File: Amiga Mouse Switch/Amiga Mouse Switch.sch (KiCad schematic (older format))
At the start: 23 parts, among them J1 JOYSTICK, J2 Mouse, J3 Amiga IDC, M1 Mounting, M2 Mounting, M3 Mounting, M4 Mounting, SW1 JOY_SEL, SW2 MOUSE_SEL, U1 74HCT4053, U2 74HCT4053, U3 NE555

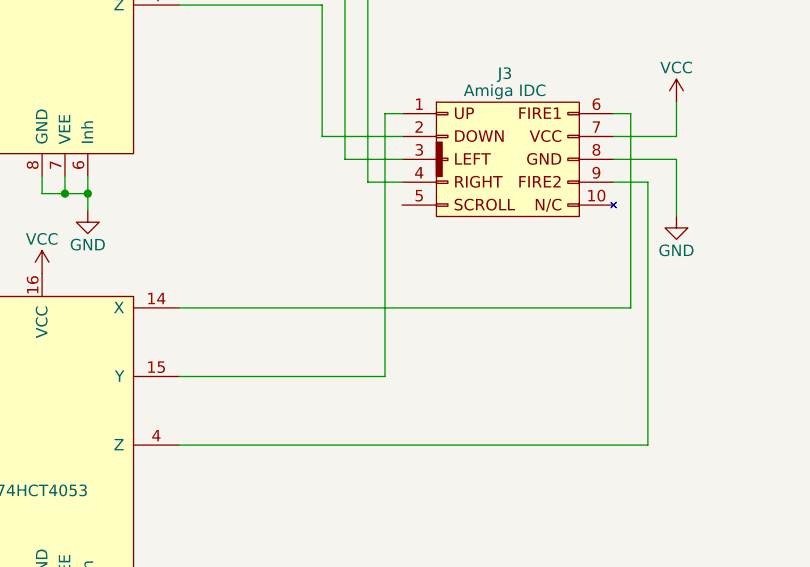
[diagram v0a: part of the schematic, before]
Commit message: Added diode for lines that have pull-ups onboard
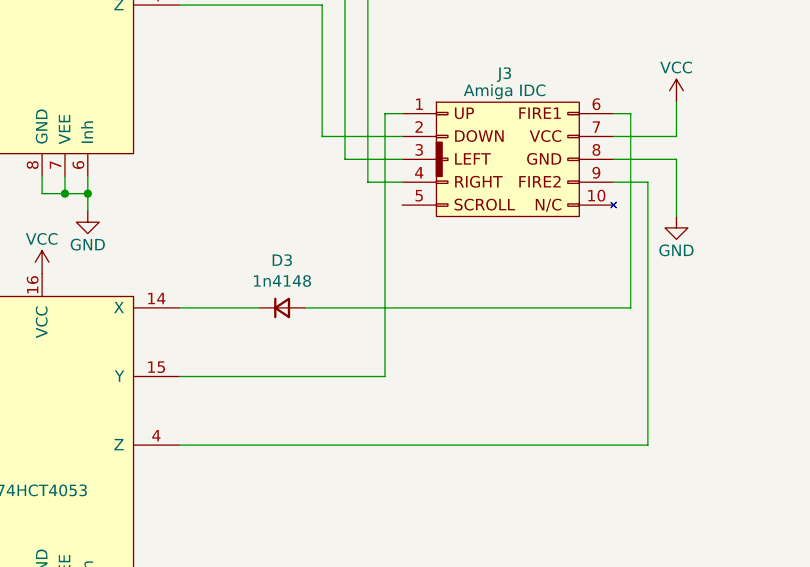
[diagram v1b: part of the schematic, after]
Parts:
- added D3: 1n4148, Diode_THT:D_DO-35_SOD27_P7.62mm_Horizontal, symbol Device:D_Small
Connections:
- net at U2.14 (X): now also D3.1 (K); no longer J3.6 (Pin_6)
- new net: D3.2 (A), J3.6 (Pin_6)
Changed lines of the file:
@@
 	6550 2475 6475 2475
 Wire Wire Line
-	4575 3325 6550 3325
+	4575 3325 4925 3325
 Wire Wire Line
 	6475 2775 6625 2775
@@
 Wire Wire Line
 	3525 6325 2600 6325
+$Comp
+L Device:D_Small D3
+U 1 1 604A3E07
+P 5025 3325
+F 0 "D3" H 5025 3532 50  0000 C CNN
+F 1 "1n4148" H 5025 3441 50  0000 C CNN
+F 2 "Diode_THT:D_DO-35_SOD27_P7.62mm_Horizontal" V 5025 3325 50  0001 C CNN
+F 3 "~" V 5025 3325 50  0001 C CNN
+	1    5025 3325
+	1    0    0    -1
+$EndComp
+Wire Wire Line
+	5125 3325 6550 3325
 $EndSCHEMATC

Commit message: Fixed RMB
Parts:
- added D4: 1n4148, Diode_THT:D_DO-35_SOD27_P7.62mm_Horizontal, symbol Device:D_Small
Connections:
- net FIRE2: now also J3.9 (Pin_9), D4.2 (A); no longer U2.3 (Z1)
- net GND: now also U2.3 (Z1), U2.5 (Z0)
- net RMB: now also D4.1 (K); no longer U2.5 (Z0)
- net at U2.4 (Z): no longer J3.9 (Pin_9)
- no-connect marks 2 -> 3
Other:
- moved on the sheet: D1, D2, D3, J1, J2, J3, JP1, JP2, R1, R2, R3, R4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

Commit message: Added README
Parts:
- R3, R4: value 220 -> 330
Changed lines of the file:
@@
 P 5700 6975
 F 0 "R4" V 5780 6975 50  0000 C CNN
-F 1 "220" V 5700 6975 50  0000 C CNN
+F 1 "330" V 5700 6975 50  0000 C CNN
 F 2 "Resistor_THT:R_Axial_DIN0207_L6.3mm_D2.5mm_P10.16mm_Horizontal" V 5630 6975 50  0001 C CNN
 F 3 "" H 5700 6975 50  0001 C CNN
@@
 P 5700 5825
 F 0 "R3" V 5780 5825 50  0000 C CNN
-F 1 "220" V 5700 5825 50  0000 C CNN
+F 1 "330" V 5700 5825 50  0000 C CNN
 F 2 "Resistor_THT:R_Axial_DIN0207_L6.3mm_D2.5mm_P10.16mm_Horizontal" V 5630 5825 50  0001 C CNN
 F 3 "" H 5700 5825 50  0001 C CNN

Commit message: Tweaks for RMB (untested)
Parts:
- removed D4: 1n4148, Diode_THT:D_DO-35_SOD27_P7.62mm_Horizontal, symbol Device:D_Small
- added JP3: EN_SCROLL, solder_bridge:bridge, symbol Jumper:SolderJumper_2_Bridged
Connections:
- net RMB: now also J3.9 (Pin_9)
- net SCROLL: now reaches J2.5 (SCROLL)
- net SCROLL: now also JP3.1 (A)
- net at J3.5 (Pin_5): now also JP3.2 (B)
- net FIRE2: no longer names the net of J1.9
- net FIRE2: no longer J3.9 (Pin_9)
- no-connect marks 3 -> 4
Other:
- note added: "Revision C:\nRevision B had issues with some machines not having a working\nRMB, diode D4 was removed along with pin 9 of the joystick port.\nThe latter part as a preventative measure as a mouse includes\ncomponents that may or may not like having its outputs shorted\nout via the joystick."
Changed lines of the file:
@@
 Title "Amiga Mouse/Joystick Switch"
 Date ""
-Rev "A"
+Rev "C"
 Comp ""
 Comment1 ""
@@
 L power:VCC #PWR011
 U 1 1 5D11F85F
-P 1625 975
-F 0 "#PWR011" H 1625 825 50  0001 C CNN
-F 1 "VCC" H 1625 1125 50  0000 C CNN
-F 2 "" H 1625 975 50  0001 C CNN
-F 3 "" H 1625 975 50  0001 C CNN
-	1    1625 975
+P 1625 675
+F 0 "#PWR011" H 1625 525 50  0001 C CNN
+F 1 "VCC" H 1625 825 50  0000 C CNN
+F 2 "" H 1625 675 50  0001 C CNN
+F 3 "" H 1625 675 50  0001 C CNN
+	1    1625 675
 	1    0    0    -1
 $EndComp
@@
 	1475 1400 1550 1400
 Wire Wire Line
-	2500 800  1775 800
-Wire Wire Line
 	1775 800  1775 1200
 Wire Wire Line
 	1775 1200 1475 1200
-Wire Wire Line
-	1475 3125 1825 3125
-Wire Wire Line
-	1825 3125 1825 3925
-Wire Wire Line
-	1825 3925 2500 3925
 Wire Notes Line
 	3375 7675 3375 5225
@@
 	1475 1600 1625 1600
 Wire Wire Line
-	1625 1600 1625 975
-Wire Wire Line
 	1625 2900 1625 3525
 Wire Wire Line
@@
 Wire Wire Line
 	1550 3325 1550 3975
-Text Label 1800 800  0    50   ~ 0
-RMB
-Text Label 1850 3925 0    50   ~ 0
-FIRE2
 Text Label 3350 3225 2    50   ~ 0
 UP
@@
 	4575 2825 4925 2825
 Wire Wire Line
-	6475 2275 6625 2275
-Wire Wire Line
 	6475 2175 6750 2175
 Wire Wire Line
@@
 	1    0    0    -1
 $EndComp
-$Comp
-L Device:D_Small D4
-U 1 1 605041F3
-P 2500 1750
-F 0 "D4" H 2500 1957 50  0000 C CNN
-F 1 "1n4148" H 2500 1866 50  0000 C CNN
-F 2 "Diode_THT:D_DO-35_SOD27_P7.62mm_Horizontal" V 2500 1750 50  0001 C CNN
-F 3 "~" V 2500 1750 50  0001 C CNN
-	1    2500 1750
-	0    1    1    0
-$EndComp
-Wire Wire Line
-	2500 1650 2500 800
 Wire Wire Line
 	2300 2825 2300 6800
@@
 	2600 3725 2600 6400
 Connection ~ 2600 3725
-Wire Wire Line
-	2500 1850 2500 3925
-Wire Wire Line
-	2500 3925 2500 4725
-Wire Wire Line
-	2500 4725 6625 4725
-Connection ~ 2500 3925
-Wire Wire Line
-	6625 2275 6625 4725
 NoConn ~ 4575 3425
 Wire Wire Line
@@
 Wire Wire Line
 	3300 3525 3375 3525
+NoConn ~ 1475 3125
+Text Notes 7500 2275 0    50   ~ 0
+Revision C:\nRevision B had issues with some machines not having a working\nRMB, diode D4 was removed along with pin 9 of the joystick port.\nThe latter part as a preventative measure as a mouse includes\ncomponents that may or may not like having its outputs shorted\nout via the joystick.
+Text GLabel 1925 800  2    60   Output ~ 0
+RMB
+Text GLabel 6875 2275 2    60   Input ~ 0
+RMB
+Wire Wire Line
+	6475 2275 6875 2275
+Wire Wire Line
+	1925 800  1775 800
+Text GLabel 1925 675  2    60   Output ~ 0
+SCROLL
+Wire Wire Line
+	1475 1100 1700 1100
+Wire Wire Line
+	1700 1100 1700 675
+Wire Wire Line
+	1700 675  1925 675
+Wire Wire Line
+	1625 675  1625 1600
+Text GLabel 4925 2375 0    60   Input ~ 0
+SCROLL
+$Comp
+L Jumper:SolderJumper_2_Bridged JP3
+U 1 1 655EC11E
+P 5150 2375
+F 0 "JP3" H 5150 2580 50  0000 C CNN
+F 1 "EN_SCROLL" H 5150 2489 50  0000 C CNN
+F 2 "solder_bridge:bridge" H 5150 2375 50  0001 C CNN
+F 3 "~" H 5150 2375 50  0001 C CNN
+	1    5150 2375
+	1    0    0    -1
+$EndComp
+Wire Wire Line
+	4925 2375 5000 2375
+Wire Wire Line
+	5300 2375 5550 2375
 $EndSCHEMATC
